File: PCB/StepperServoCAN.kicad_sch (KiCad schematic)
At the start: 136 parts, among them J1 CAR, J2 Debug, J3 Motor, J4 Conn_01x06, Q1 AO3401A, Q2 2N7002, Q3 AO3401A, SW1 Rst, SW2 Fcn>, SW3 Fcn>, U1 AH1806-W, U2 STM32F103CBT6, U3 LMV321, U4 DRV8870, U5 DRV8870, U6 LMV321, U7 TLE5012B, U8 TMAG5170-Q1, U9 SN65HVD230, Y1 16Mhz 9pF

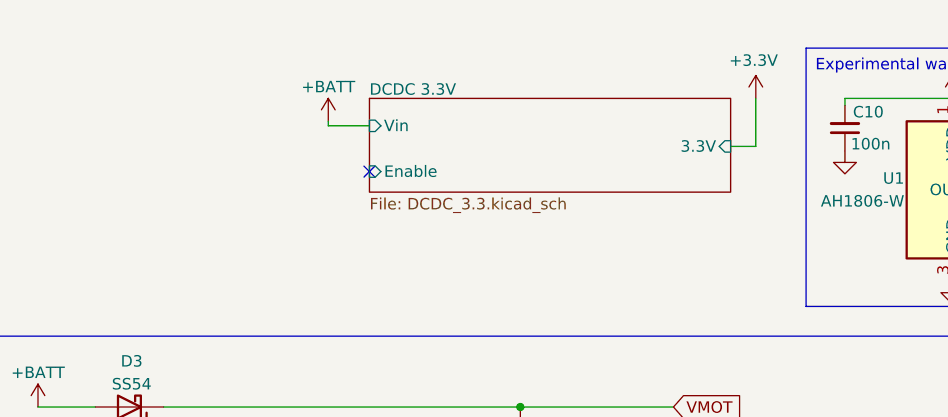
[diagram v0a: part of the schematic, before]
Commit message: Added 3.3v tap point.
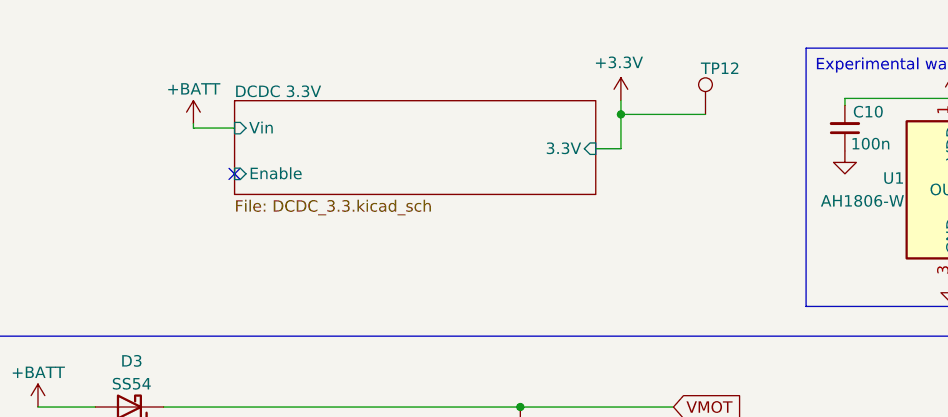
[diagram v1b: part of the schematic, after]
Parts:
- added TP12: Pad, TestPoint:TestPoint_Pad_D1.0mm, symbol Connector:TestPoint
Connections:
- net +3.3V: now also TP12.1
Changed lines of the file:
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@@
   (junction (at 153.67 135.89) (diameter 0) (color 0 0 0 0)
   )
+  (junction (at 86.106 23.876) (diameter 0) (color 0 0 0 0)
+  )
   (junction (at 203.962 63.5) (diameter 0) (color 0 0 0 0)
   )
@@
   (junction (at 74.93 56.388) (diameter 0) (color 0 0 0 0)
   )
-  (no_connect (at 58.166 30.226))
+  (no_connect (at 43.18 30.48))
   (no_connect (at 223.012 161.798))
   (no_connect (at 230.632 161.798))
@@
     (stroke (width 0) (type default))
   )
+  (wire (pts (xy 86.106 23.876) (xy 86.106 22.352))
+    (stroke (width 0) (type default))
+  )
   (polyline (pts (xy 85.09 157.48) (xy 85.09 194.31))
     (stroke (width 0) (type default))
@@
     (stroke (width 0) (type default))
   )
+  (wire (pts (xy 86.106 23.876) (xy 95.504 23.876))
+    (stroke (width 0) (type default))
+  )
   (wire (pts (xy 128.27 169.672) (xy 128.27 170.942))
     (stroke (width 0) (type default))
@@
     (stroke (width 0) (type default))
   )
-  (wire (pts (xy 53.594 25.146) (xy 58.166 25.146))
+  (wire (pts (xy 38.608 25.4) (xy 43.18 25.4))
     (stroke (width 0) (type default))
   )
@@
     (stroke (width 0) (type default))
   )
-  (wire (pts (xy 98.298 27.432) (xy 101.092 27.432))
+  (wire (pts (xy 83.312 27.686) (xy 86.106 27.686))
     (stroke (width 0) (type default))
   )
@@
     (stroke (width 0) (type default))
   )
-  (wire (pts (xy 53.594 25.146) (xy 53.594 24.638))
+  (wire (pts (xy 38.608 25.4) (xy 38.608 24.892))
     (stroke (width 0) (type default))
   )
@@
     (stroke (width 0) (type default))
   )
-  (wire (pts (xy 101.092 27.432) (xy 101.092 22.098))
+  (wire (pts (xy 86.106 27.686) (xy 86.106 23.876))
     (stroke (width 0) (type default))
   )
@@
     )
   )
-  (symbol (lib_id "power:+3.3V") (at 101.092 22.098 0) (unit 1)
+  (symbol (lib_id "power:+3.3V") (at 86.106 22.352 0) (unit 1)
     (in_bom yes) (on_board yes) (dnp no)
-    (property "Reference" "#PWR06" (at 101.092 25.908 0)
+    (property "Reference" "#PWR06" (at 86.106 26.162 0)
       (effects (font (size 1.27 1.27)) hide)
     )
-    (property "Value" "+3.3V" (at 100.8439 17.8901 0)
+    (property "Value" "+3.3V" (at 85.8579 18.1441 0)
       (effects (font (size 1.27 1.27)))
     )
-    (property "Footprint" "" (at 101.092 22.098 0)
+    (property "Footprint" "" (at 86.106 22.352 0)
       (effects (font (size 1.27 1.27)) hide)
     )
-    (property "Datasheet" "" (at 101.092 22.098 0)
+    (property "Datasheet" "" (at 86.106 22.352 0)
       (effects (font (size 1.27 1.27)) hide)
     )
@@
     )
   )
-  (symbol (lib_id "power:+BATT") (at 53.594 24.638 0) (unit 1)
+  (symbol (lib_id "power:+BATT") (at 38.608 24.892 0) (unit 1)
     (in_bom yes) (on_board yes) (dnp no)
-    (property "Reference" "#PWR011" (at 53.594 28.448 0)
+    (property "Reference" "#PWR011" (at 38.608 28.702 0)
       (effects (font (size 1.27 1.27)) hide)
     )
-    (property "Value" "+BATT" (at 53.594 20.828 0)
+    (property "Value" "+BATT" (at 38.608 21.082 0)
       (effects (font (size 1.27 1.27)))
     )
-    (property "Footprint" "" (at 53.594 24.638 0)
+    (property "Footprint" "" (at 38.608 24.892 0)
       (effects (font (size 1.27 1.27)) hide)
     )
-    (property "Datasheet" "" (at 53.594 24.638 0)
+    (property "Datasheet" "" (at 38.608 24.892 0)
       (effects (font (size 1.27 1.27)) hide)
     )
@@
     )
   )
+  (symbol (lib_id "Connector:TestPoint") (at 95.504 23.876 0) (unit 1)
+    (in_bom yes) (on_board yes) (dnp no)
+    (property "Reference" "TP12" (at 94.996 18.796 0)
+      (effects (font (size 1.27 1.27)) (justify left))
+    )
+    (property "Value" "Pad" (at 92.964 18.796 0)
+      (effects (font (size 1.27 1.27)) (justify left) hide)
+    )
+    (property "Footprint" "TestPoint:TestPoint_Pad_D1.0mm" (at 100.584 23.876 0)
+      (effects (font (size 1.27 1.27)) hide)
+    )
+    (property "Datasheet" "~" (at 100.584 23.876 0)
+      (effects (font (size 1.27 1.27)) hide)
+    )
+    (pin "1")
+    (instances
+      (project "StepperServoCAN"
+        (path "/92dad13e-412a-43d4-9260-9087579302b1"
+          (reference "TP12") (unit 1)
+        )
+      )
+    )
+  )
   (symbol (lib_id "Device:C_Small") (at 225.298 23.114 270) (unit 1)
     (in_bom yes) (on_board yes) (dnp no)
@@
     )
   )
-  (sheet (at 58.166 22.098) (size 40.132 10.414)
+  (sheet (at 43.18 22.352) (size 40.132 10.414)
     (stroke (width 0.1524) (type solid))
     (fill (color 0 0 0 0.0000))
-    (property "Sheetname" "DCDC 3.3V" (at 58.166 21.844 0)
+    (property "Sheetname" "DCDC 3.3V" (at 43.18 22.098 0)
       (effects (font (size 1.27 1.27)) (justify left bottom))
     )
-    (property "Sheetfile" "DCDC_3.3.kicad_sch" (at 58.166 33.0966 0)
+    (property "Sheetfile" "DCDC_3.3.kicad_sch" (at 43.18 33.3506 0)
       (effects (font (size 1.27 1.27)) (justify left top))
     )
-    (pin "3.3V" input (at 98.298 27.432 0)
+    (pin "3.3V" input (at 83.312 27.686 0)
       (effects (font (size 1.27 1.27)) (justify right))
     )
-    (pin "Vin" input (at 58.166 25.146 180)
+    (pin "Vin" input (at 43.18 25.4 180)
       (effects (font (size 1.27 1.27)) (justify left))
     )
-    (pin "Enable" input (at 58.166 30.226 180)
+    (pin "Enable" input (at 43.18 30.48 180)
       (effects (font (size 1.27 1.27)) (justify left))
     )

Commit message: Versioning. Connectors center pos for fab.
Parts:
- J4, U8: now left out of the parts list
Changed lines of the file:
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@@
   (title_block
     (title "StepperServoCAN")
-    (rev "0.2")
+    (rev "0.3")
     (company "RetroPilot")
     (comment 1 "Licensed under CERN-OHL-S v2")
@@
   )
   (symbol (lib_id "Connector_Generic:Conn_01x06") (at 270.51 147.32 0) (mirror x) (unit 1)
-    (in_bom yes) (on_board yes) (dnp no)
+    (in_bom no) (on_board yes) (dnp no)
     (property "Reference" "J4" (at 270.002 149.606 0)
       (effects (font (size 1.27 1.27)) (justify left))
@@
   )
   (symbol (lib_id "Sensor_Magnetic:TMAG5170-Q1") (at -25.4 179.578 0) (unit 1)
-    (in_bom yes) (on_board yes) (dnp yes)
+    (in_bom no) (on_board yes) (dnp yes)
     (property "Reference" "U8" (at -15.494 165.1 0)
       (effects (font (size 1.27 1.27)))

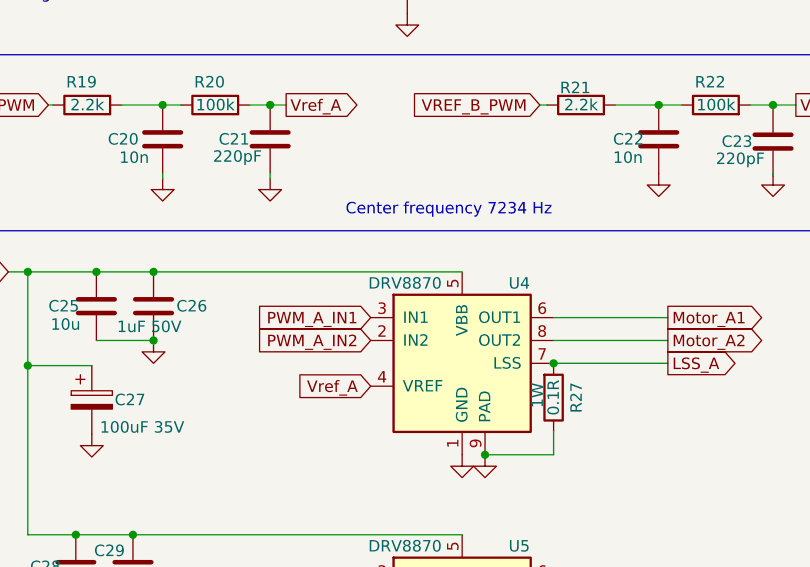
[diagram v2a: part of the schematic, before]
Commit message: Using low-rds on AT8236
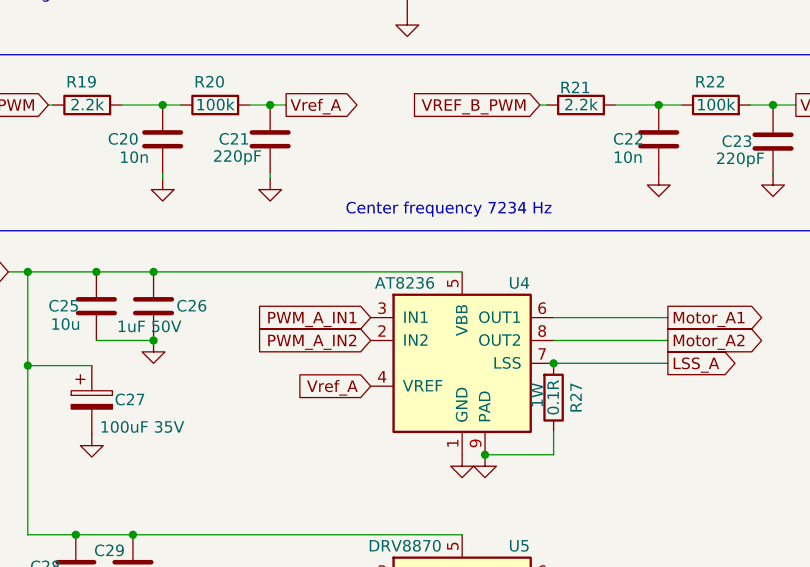
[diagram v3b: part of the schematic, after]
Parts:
- U4: value DRV8870 -> AT8236; LCSC C86590 -> C2827823
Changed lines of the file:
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@@
       (effects (font (size 1.27 1.27)))
     )
-    (property "Value" "DRV8870" (at 74.676 93.98 0)
+    (property "Value" "AT8236" (at 74.676 93.98 0)
       (effects (font (size 1.27 1.27)))
     )
@@
       (effects (font (size 1.27 1.27)) hide)
     )
-    (property "Datasheet" "https://www.ti.com/lit/ds/symlink/drv8870.pdf" (at 73.406 93.98 0)
+    (property "Datasheet" "https://wmsc.lcsc.com/wmsc/upload/file/pdf/v2/lcsc/2109242230_ZHONGKEWEI-AT8236_C2827823.pdf" (at 73.406 93.98 0)
       (effects (font (size 1.27 1.27)) hide)
     )
-    (property "LCSC" "C86590" (at 87.376 93.98 0)
+    (property "LCSC" "C2827823" (at 87.376 93.98 0)
       (effects (font (size 1.27 1.27)) hide)
     )

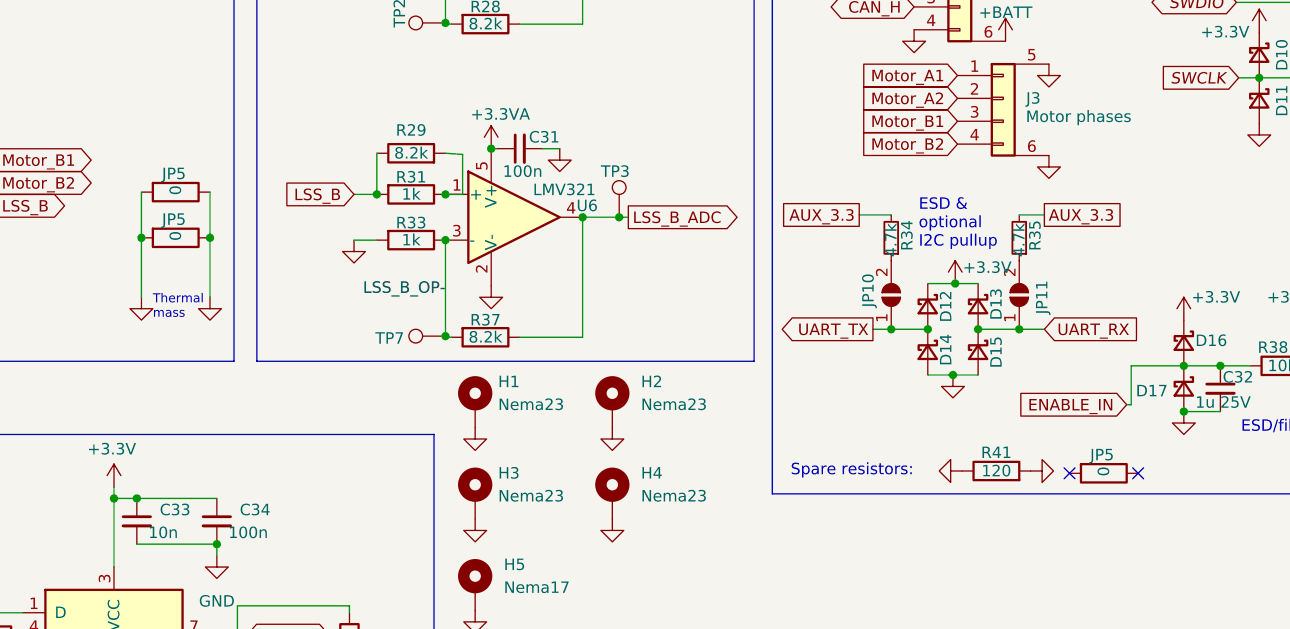
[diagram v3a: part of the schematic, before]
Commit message: Kicad8. Also clear zone filling before saving
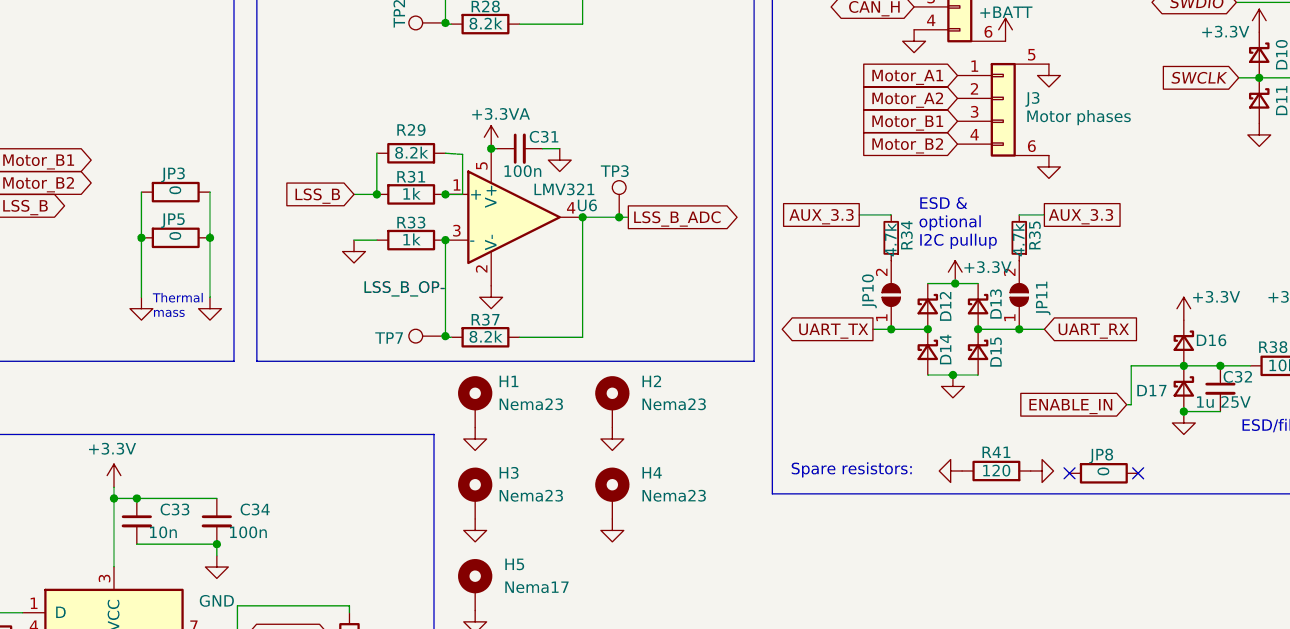
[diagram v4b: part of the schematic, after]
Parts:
- FB1: value FerriteBead 200mA -> FerriteBead 200mA
- renumbered JP5 to JP3, JP5 to JP8

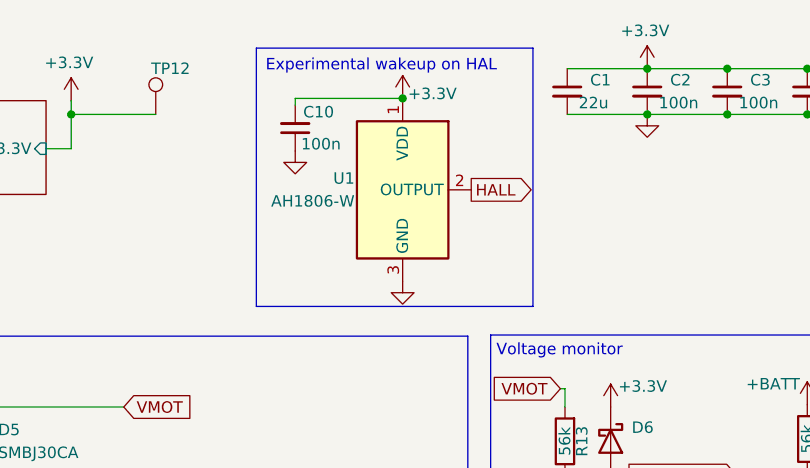
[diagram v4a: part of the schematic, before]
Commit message: removed hal test circuit and spare soic-8
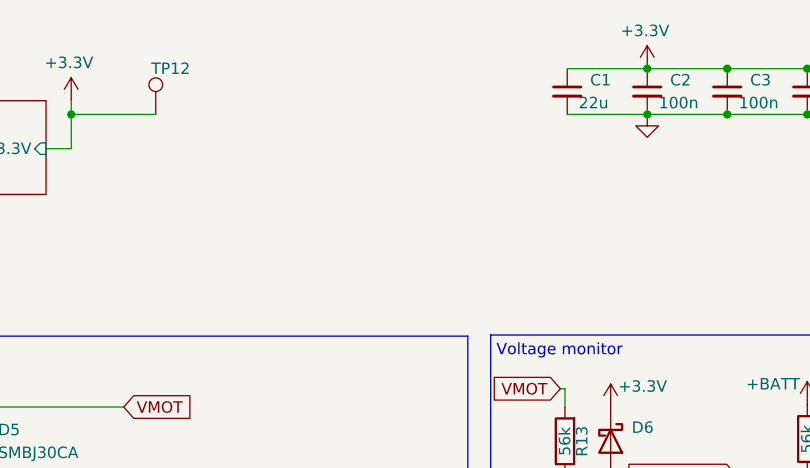
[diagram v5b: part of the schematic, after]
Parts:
- removed C10: 100n, Capacitor_SMD:C_0402_1005Metric, symbol Device:C_Small
- removed U1: AH1806-W, Package_TO_SOT_SMD:SC-59, symbol Sensor_Magnetic:AH1806-W

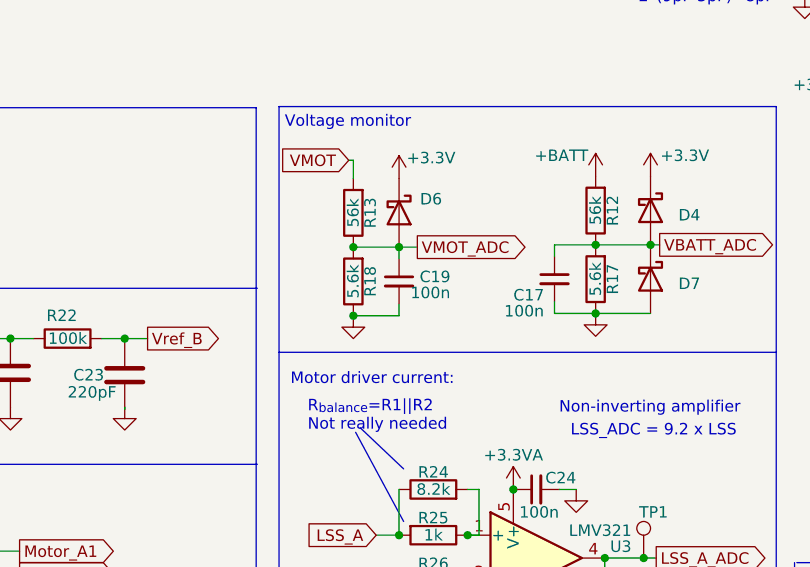
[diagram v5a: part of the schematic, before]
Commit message: removed vmot adc filtering cap
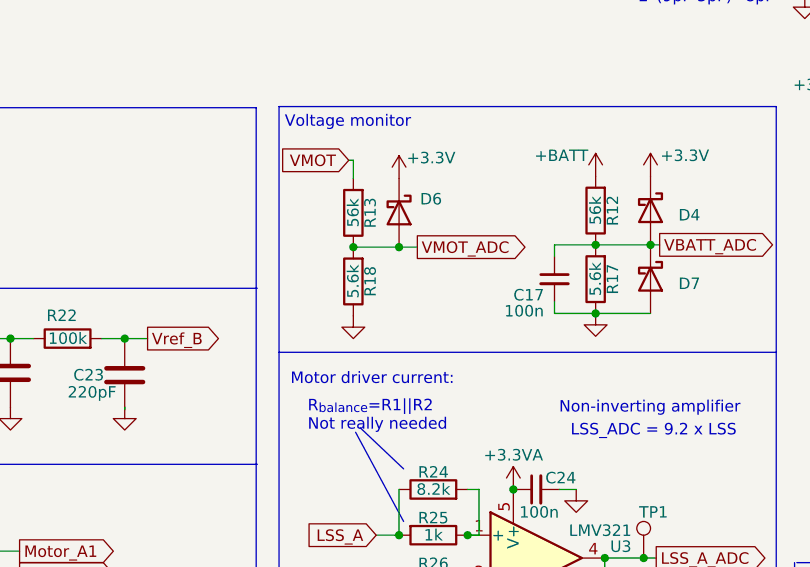
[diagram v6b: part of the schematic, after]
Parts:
- removed C19: 100n, Capacitor_SMD:C_0402_1005Metric, symbol Device:C_Small
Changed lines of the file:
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@@
 	)
 	(junction
-		(at 140.97 71.628)
-		(diameter 0)
-		(color 0 0 0 0)
-	)
-	(junction
 		(at 128.27 169.672)
 		(diameter 0)
@@
 	(wire
 		(pts
-			(xy 146.05 70.358) (xy 146.05 71.628)
-		)
-		(stroke
-			(width 0)
-			(type default)
-		)
-	)
-	(wire
-		(pts
 			(xy 212.09 63.5) (xy 212.09 65.024)
 		)
@@
 	(wire
 		(pts
-			(xy 146.05 71.628) (xy 140.97 71.628)
-		)
-		(stroke
-			(width 0)
-			(type default)
-		)
-	)
-	(wire
-		(pts
 			(xy 266.446 77.978) (xy 265.43 77.978)
 		)
@@
 	(wire
 		(pts
-			(xy 146.05 65.278) (xy 146.05 64.008)
-		)
-		(stroke
-			(width 0)
-			(type default)
-		)
-	)
-	(wire
-		(pts
 			(xy 46.736 92.71) (xy 81.026 92.71)
 		)
@@
 					(unit 1)
 				)
-			)
-		)
-	)
-	(symbol
-		(lib_id "Device:C_Small")
-		(at 146.05 67.818 0)
-		(unit 1)
-		(exclude_from_sim no)
-		(in_bom yes)
-		(on_board yes)
-		(dnp no)
-		(property "Reference" "C19"
-			(at 148.336 67.31 0)
-			(effects
-				(font
-					(size 1.27 1.27)
-				)
-				(justify left)
-			)
-		)
-		(property "Value" "100n"
-			(at 147.32 69.088 0)
-			(effects
-				(font
-					(size 1.27 1.27)
-				)
-				(justify left)
-			)
-		)
-		(property "Footprint" "Capacitor_SMD:C_0402_1005Metric"
-			(at 146.05 67.818 0)
-			(effects
-				(font
-					(size 1.27 1.27)
-				)
-				(hide yes)
-			)
-		)
-		(property "Datasheet" "https://weblib.samsungsem.com/mlcc/mlcc-ec-data-sheet.do?partNumber=CL05B104KO5NNN"
-			(at 146.05 67.818 0)
-			(effects
-				(font
-					(size 1.27 1.27)
-				)
-				(hide yes)
-			)
-		)
-		(property "Description" ""
-			(at 146.05 67.818 0)
-			(effects
-				(font
-					(size 1.27 1.27)
-				)
-				(hide yes)
-			)
-		)
-		(property "LCSC" "C1525"
-			(at 148.59 66.5542 0)
-			(effects
-				(font
-					(size 1.27 1.27)
-				)
-				(hide yes)
-			)
-		)
-		(pin "1"
-		)
-		(pin "2"
-		)
-		(instances
-			(project "StepperServoCAN"
-				(path "/92dad13e-412a-43d4-9260-9087579302b1"
-					(reference "C19")
-					(unit 1)
-				)

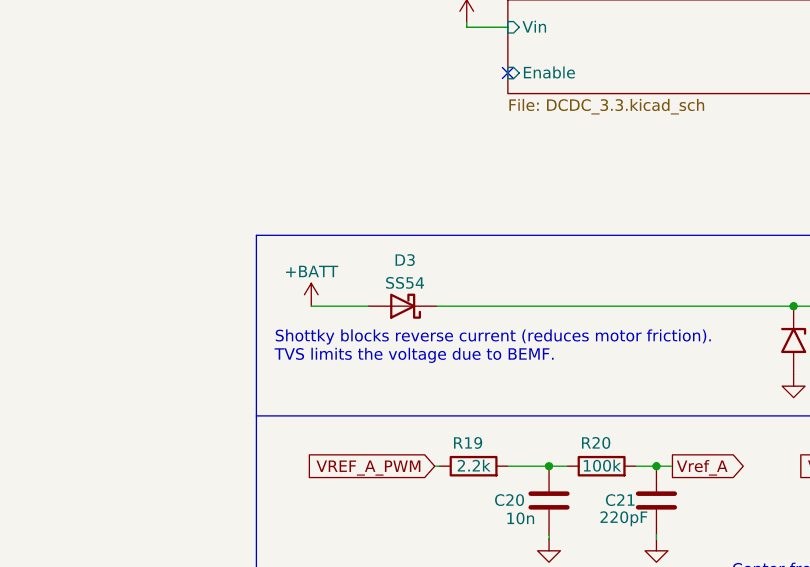
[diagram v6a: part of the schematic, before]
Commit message: Lower voltage-drop schottky
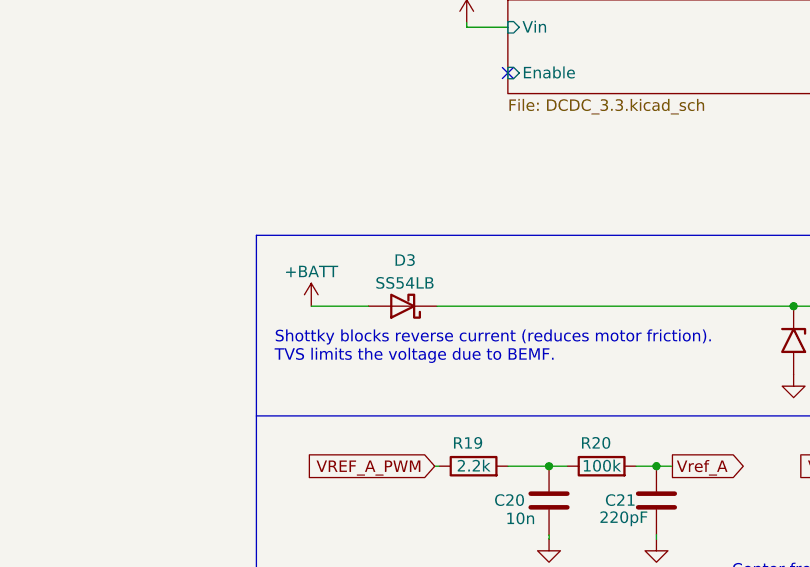
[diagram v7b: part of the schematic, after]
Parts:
- D3: value SS54 -> SS54LB; Field6 (none) -> Alternative SS54L - 450mV@5A; LCSC C22452 -> C7450527
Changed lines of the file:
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@@
 			)
 		)
-		(property "Value" "SS54"
+		(property "Value" "SS54LB"
 			(at 31.75 53.848 0)
 			(effects
@@
 			)
 		)
-		(property "LCSC" "C22452"
+		(property "LCSC" "C7450527"
 			(at 31.496 56.388 0)
 			(effects
+				(font
+					(size 1.27 1.27)
+				)
+				(hide yes)
+			)
+		)
+		(property "Field6" "Alternative SS54L - 450mV@5A"
+			(at 31.496 56.388 0)
+			(effects
